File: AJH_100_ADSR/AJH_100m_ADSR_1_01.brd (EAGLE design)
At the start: 19 x 106.8 mm, 66 parts, among them IC1 TL072D, IC2 TL072D, J100 PJ301_THONKICONN6, J101 PJ301_THONKICONN6, J102 PJ301_THONKICONN6, Q1 MMBT3904, Q10 MMBT3904, Q2 MMBT3906, Q3 MMBT3906, Q4 MMBT3904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

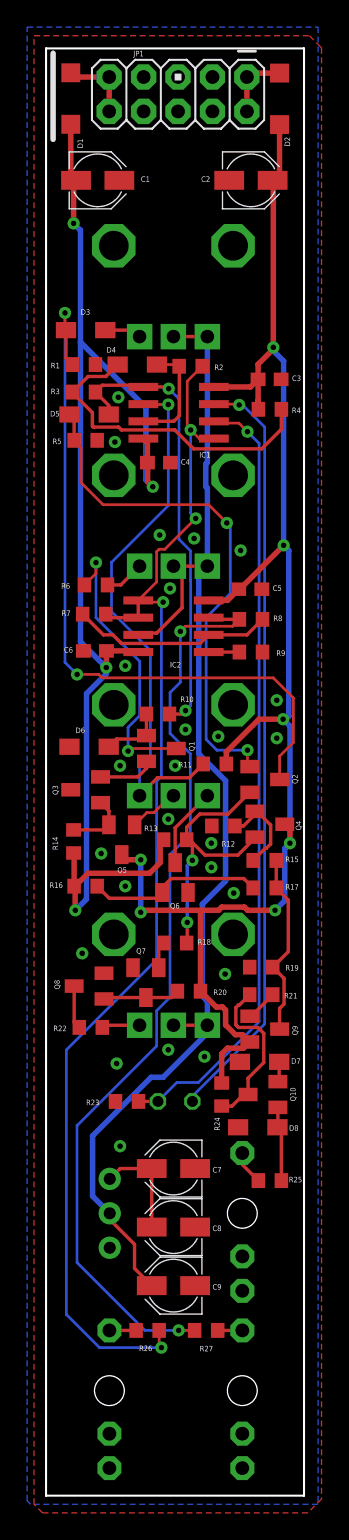
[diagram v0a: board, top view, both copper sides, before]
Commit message: Updated a100  adsr with correct pot direction
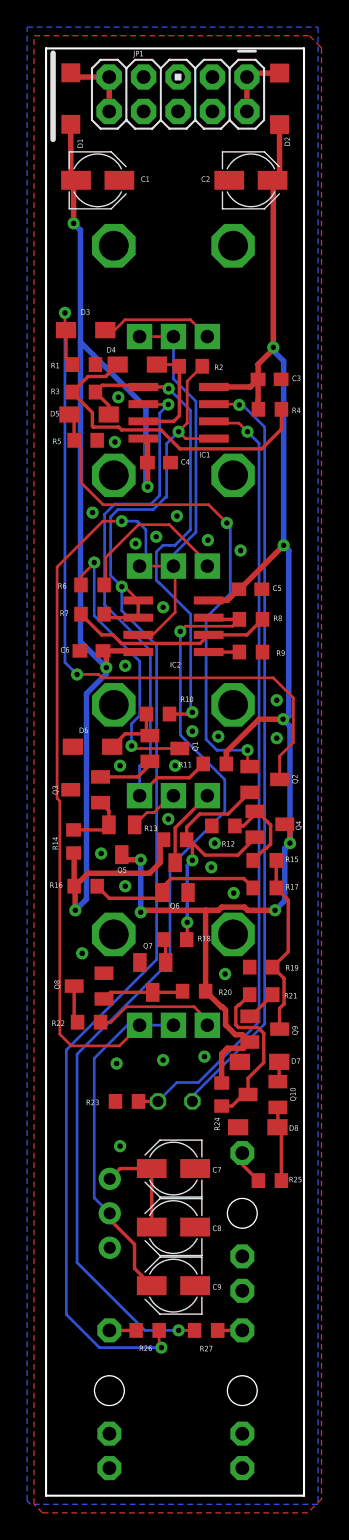
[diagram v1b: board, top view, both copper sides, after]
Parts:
- moved Q7 0.64 mm to (7.87, 38.2)
- moved R22 0.40 mm to (3.17, 34.9)
- moved R20 0.38 mm to (10.9, 37.2)
- moved C6 0.25 mm to (3.35, 62.3)
- moved D6 0.25 mm to (3.43, 55.2)
- moved R6 0.25 mm to (3.43, 67.2)
- moved Q1 0.25 mm to (8.76, 55.1)
- moved R18 0.25 mm to (9.53, 41.0)
- moved R7 0.13 mm to (3.43, 65.0)
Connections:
- removed net N$36: D3.C, R100.P$1
- removed net N$56: R101.P$1, R6.1
- removed net N$60: R103.P$1, R22.1
- new net N$5: D3.C, R100.P$3
- new net N$7: R101.P$3, R6.1
- new net N$8: R103.P$3, R22.1
- net N$38: now also R100.P$1, R101.P$1, R103.P$1; no longer R100.P$3, R101.P$3, R103.P$3
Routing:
- net N$38: track 92.8 -> 108.1 mm, vias 0 -> 1
- net N$7: track 0.00 -> 12.0 mm
- net N$8: track 0.00 -> 9.14 mm
- net N$5: track 0.00 -> 8.36 mm
- net N$10: track 92.4 -> 96.2 mm, vias 4 -> 3
- net N$32: track 33.6 -> 36.7 mm
- net N$56: track 2.94 -> 0.00 mm
- net N$60: track 2.81 -> 0.00 mm
- net N$36: track 2.72 -> 0.00 mm
- net N$27: track 39.6 -> 41.6 mm
- net N$13: track 68.7 -> 70.2 mm
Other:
- board text added: "140 ADSR v1.01 Copyright forestcaver 2020"
- board text removed: "140 ADSR v1.0 Copyright forestcaver 2020"
